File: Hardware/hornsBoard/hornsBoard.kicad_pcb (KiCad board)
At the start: 2 copper layers, 24 x 27 mm, 10 parts, among them J1 Conn_01x03, J2 Conn_01x02, J3 Conn_01x02, J4 Conn_01x02, Q2 IRF6785

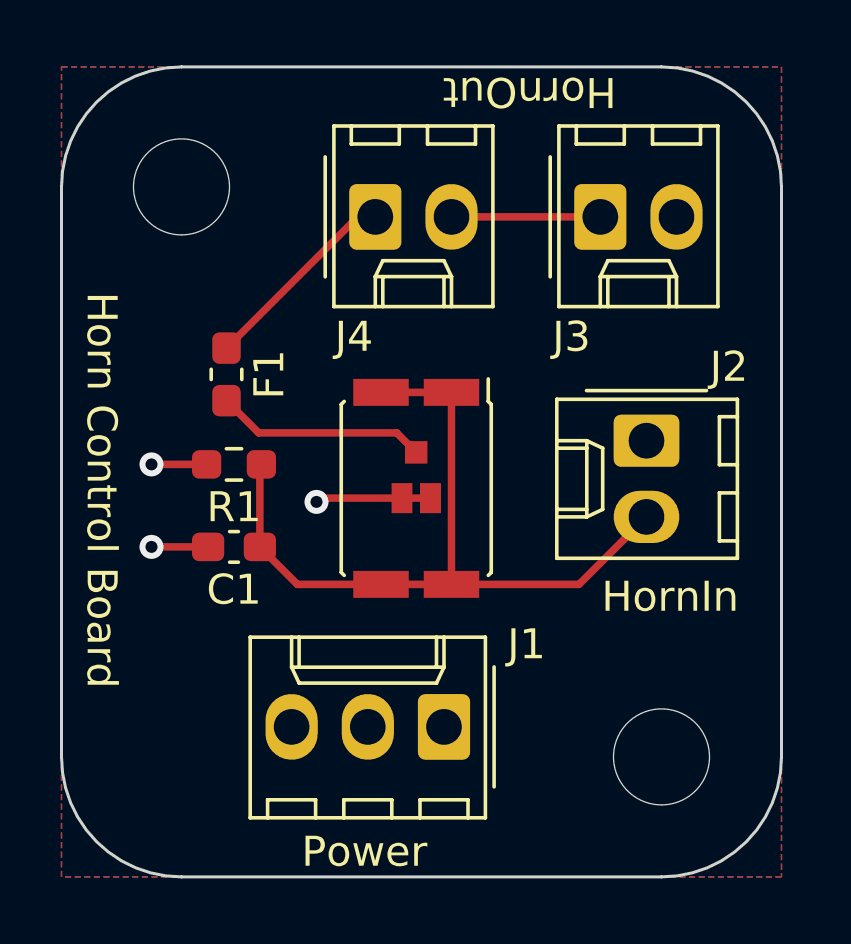
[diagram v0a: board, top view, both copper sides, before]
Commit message: reworked hornsBoard PCB
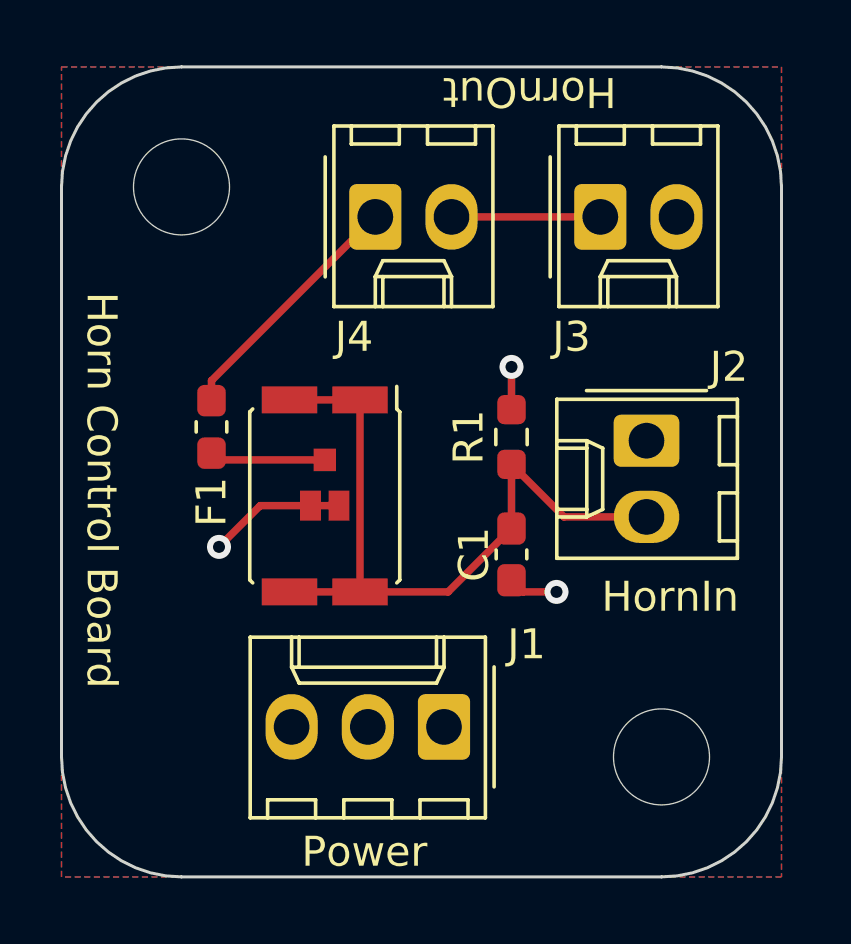
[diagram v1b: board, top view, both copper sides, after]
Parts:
- moved R1 9.29 mm to (153.0, 109.3), turned to 90 degrees
- moved C1 9.25 mm to (153.0, 113.2), turned to -90 degrees
- moved Q2 3.06 mm to (146.8, 111.3)
- moved F1 1.82 mm to (143.0, 109.0)
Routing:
- net Net-(Q2-G): track 7.04 -> 3.87 mm
- net Net-(J4-Pin_1): track 6.77 -> 8.97 mm
- net /Horn_Signal: track 25.9 -> 24.4 mm
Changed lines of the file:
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@@
   )
   (footprint "Resistor_SMD:R_0603_1608Metric_Pad0.98x0.95mm_HandSolder" (layer "F.Cu")
-    (at 143.75 110.25 180)
+    (at 153 109.3375 90)
     (descr "Resistor SMD 0603 (1608 Metric), square (rectangular) end terminal, IPC_7351 nominal with elongated pad for handsoldering. (Body size source: IPC-SM-782 page 72, https://www.pcb-3d.com/wordpress/wp-content/uploads/ipc-sm-782a_amendment_1_and_2.pdf), generated with kicad-footprint-generator")
     (tags "resistor handsolder")
@@
     (property "ki_keywords" "R res resistor")
     (attr smd)
-    (fp_text reference "R1" (at 0 -1.43) (layer "F.SilkS")
-        (effects (font (size 1 1) (thickness 0.15)))
-    )
-    (fp_text value "R_US" (at 0 1.43) (layer "F.Fab") hide
-        (effects (font (size 1 1) (thickness 0.15)))
-    )
-    (fp_text user "${REFERENCE}" (at 0 0) (layer "F.Fab")
+    (fp_text reference "R1" (at 0 -1.43 90) (layer "F.SilkS")
+        (effects (font (size 1 1) (thickness 0.15)))
+    )
+    (fp_text value "R_US" (at 0 1.43 90) (layer "F.Fab") hide
+        (effects (font (size 1 1) (thickness 0.15)))
+    )
+    (fp_text user "${REFERENCE}" (at 0 0 90) (layer "F.Fab")
         (effects (font (size 0.4 0.4) (thickness 0.06)))
     )
@@
     (fp_line (start 0.8 0.4125) (end -0.8 0.4125)
       (stroke (width 0.1) (type solid)) (layer "F.Fab"))
-    (pad "1" smd roundrect (at -0.9125 0 180) (size 0.975 0.95) (layers "F.Cu" "F.Paste" "F.Mask") (roundrect_rratio 0.25)
+    (pad "1" smd roundrect (at -0.9125 0 90) (size 0.975 0.95) (layers "F.Cu" "F.Paste" "F.Mask") (roundrect_rratio 0.25)
       (net 1 "/Horn_Signal") (pintype "passive"))
-    (pad "2" smd roundrect (at 0.9125 0 180) (size 0.975 0.95) (layers "F.Cu" "F.Paste" "F.Mask") (roundrect_rratio 0.25)
+    (pad "2" smd roundrect (at 0.9125 0 90) (size 0.975 0.95) (layers "F.Cu" "F.Paste" "F.Mask") (roundrect_rratio 0.25)
       (net 2 "GND") (pintype "passive"))
     (model "${KICAD6_3DMODEL_DIR}/Resistor_SMD.3dshapes/R_0603_1608Metric.wrl"
@@
   )
   (footprint "Capacitor_SMD:C_0603_1608Metric_Pad1.08x0.95mm_HandSolder" (layer "F.Cu")
-    (at 143.75 113 180)
+    (at 153 113.25 -90)
     (descr "Capacitor SMD 0603 (1608 Metric), square (rectangular) end terminal, IPC_7351 nominal with elongated pad for handsoldering. (Body size source: IPC-SM-782 page 76, https://www.pcb-3d.com/wordpress/wp-content/uploads/ipc-sm-782a_amendment_1_and_2.pdf), generated with kicad-footprint-generator")
     (tags "capacitor handsolder")
@@
     (property "ki_keywords" "cap capacitor")
     (attr smd)
-    (fp_text reference "C1" (at 0 -1.43) (layer "F.SilkS")
-        (effects (font (size 1 1) (thickness 0.15)))
-    )
-    (fp_text value "C" (at 0 1.43) (layer "F.Fab") hide
-        (effects (font (size 1 1) (thickness 0.15)))
-    )
-    (fp_text user "${REFERENCE}" (at 0 0) (layer "F.Fab")
+    (fp_text reference "C1" (at 0 1.25 -270) (layer "F.SilkS")
+        (effects (font (size 1 1) (thickness 0.15)))
+    )
+    (fp_text value "C" (at 0 1.43 -270) (layer "F.Fab") hide
+        (effects (font (size 1 1) (thickness 0.15)))
+    )
+    (fp_text user "${REFERENCE}" (at 0 0 -270) (layer "F.Fab")
         (effects (font (size 0.4 0.4) (thickness 0.06)))
     )
@@
     (fp_line (start 0.8 0.4) (end -0.8 0.4)
       (stroke (width 0.1) (type solid)) (layer "F.Fab"))
-    (pad "1" smd roundrect (at -0.8625 0 180) (size 1.075 0.95) (layers "F.Cu" "F.Paste" "F.Mask") (roundrect_rratio 0.25)
+    (pad "1" smd roundrect (at -0.8625 0 270) (size 1.075 0.95) (layers "F.Cu" "F.Paste" "F.Mask") (roundrect_rratio 0.25)
       (net 1 "/Horn_Signal") (pintype "passive"))
-    (pad "2" smd roundrect (at 0.8625 0 180) (size 1.075 0.95) (layers "F.Cu" "F.Paste" "F.Mask") (roundrect_rratio 0.25)
+    (pad "2" smd roundrect (at 0.8625 0 270) (size 1.075 0.95) (layers "F.Cu" "F.Paste" "F.Mask") (roundrect_rratio 0.25)
       (net 2 "GND") (pintype "passive"))
     (model "${KICAD6_3DMODEL_DIR}/Capacitor_SMD.3dshapes/C_0603_1608Metric.wrl"
@@
   )
   (footprint "Fuse:Fuse_0603_1608Metric_Pad1.05x0.95mm_HandSolder" (layer "F.Cu")
-    (at 143.5 107.25 -90)
+    (at 143 109 -90)
     (descr "Fuse SMD 0603 (1608 Metric), square (rectangular) end terminal, IPC_7351 nominal with elongated pad for handsoldering. (Body size source: http://www.tortai-tech.com/upload/download/2011102023233369053.pdf), generated with kicad-footprint-generator")
     (tags "fuse handsolder")
@@
     (property "ki_keywords" "fuse")
     (attr smd)
-    (fp_text reference "F1" (at 0 -1.43 90) (layer "F.SilkS")
+    (fp_text reference "F1" (at 2.5 0 90) (layer "F.SilkS")
         (effects (font (size 1 1) (thickness 0.15)))
     )
@@
   )
   (footprint "Package_DirectFET:DirectFET_MZ" (layer "F.Cu")
-    (at 149.825 111.05 -90)
+    (at 146.775 111.3 -90)
     (descr "DirectFET MZ https://www.infineon.com/dgdl/Infineon-AN-1035-ApplicationNotes-v29_01-EN.pdf?fileId=5546d462533600a40153559159020f76#page=31")
     (tags "DirectFET MZ MOSFET Infineon")
@@
     (effects (font (size 1 1) (thickness 0.15)) (justify left bottom))
   )
-  (segment (start 151 107.85) (end 148.65 107.85) (width 0.25) (layer "F.Cu") (net 1))
-  (segment (start 145.8625 114.25) (end 144.6125 113) (width 0.25) (layer "F.Cu") (net 1))
-  (segment (start 155.25 114.25) (end 157.5 112) (width 0.25) (layer "F.Cu") (net 1))
-  (segment (start 144.6125 113) (end 144.6125 110.3) (width 0.25) (layer "F.Cu") (net 1))
-  (segment (start 151 107.85) (end 151 114.25) (width 0.25) (layer "F.Cu") (net 1))
-  (segment (start 148.65 114.25) (end 145.8625 114.25) (width 0.25) (layer "F.Cu") (net 1))
-  (segment (start 148.65 114.25) (end 151 114.25) (width 0.25) (layer "F.Cu") (net 1))
-  (segment (start 144.6125 110.3) (end 144.6625 110.25) (width 0.25) (layer "F.Cu") (net 1))
-  (segment (start 151 114.25) (end 155.25 114.25) (width 0.25) (layer "F.Cu") (net 1))
-  (segment (start 146.625 111.375) (end 146.5 111.5) (width 0.25) (layer "F.Cu") (net 2))
-  (segment (start 142.8875 113) (end 141 113) (width 0.25) (layer "F.Cu") (net 2))
-  (segment (start 142.8375 110.25) (end 141 110.25) (width 0.25) (layer "F.Cu") (net 2))
-  (segment (start 149.35 111.375) (end 146.625 111.375) (width 0.25) (layer "F.Cu") (net 2))
-  (segment (start 150.3 111.375) (end 149.35 111.375) (width 0.25) (layer "F.Cu") (net 2))
-  (via (at 146.5 111.5) (size 0.8) (drill 0.4) (layers "F.Cu" "B.Cu") (free) (net 2))
-  (via (at 141 113) (size 0.8) (drill 0.4) (layers "F.Cu" "B.Cu") (free) (net 2))
-  (via (at 141 110.25) (size 0.8) (drill 0.4) (layers "F.Cu" "B.Cu") (free) (net 2))
+  (segment (start 150.8875 114.5) (end 147.95 114.5) (width 0.25) (layer "F.Cu") (net 1))
+  (segment (start 153 112.3875) (end 150.8875 114.5) (width 0.25) (layer "F.Cu") (net 1))
+  (segment (start 147.95 108.1) (end 147.95 114.5) (width 0.25) (layer "F.Cu") (net 1))
+  (segment (start 147.95 114.5) (end 145.6 114.5) (width 0.25) (layer "F.Cu") (net 1))
+  (segment (start 157.5 112) (end 154.75 112) (width 0.25) (layer "F.Cu") (net 1))
+  (segment (start 154.75 112) (end 153 110.25) (width 0.25) (layer "F.Cu") (net 1))
+  (segment (start 153 110.25) (end 153 112.3875) (width 0.25) (layer "F.Cu") (net 1))
+  (segment (start 145.6 108.1) (end 147.95 108.1) (width 0.25) (layer "F.Cu") (net 1))
+  (segment (start 153.3875 114.5) (end 153 114.1125) (width 0.25) (layer "F.Cu") (net 2))
+  (segment (start 146.3 111.625) (end 144.625 111.625) (width 0.25) (layer "F.Cu") (net 2))
+  (segment (start 153 108.425) (end 153 107) (width 0.25) (layer "F.Cu") (net 2))
+  (segment (start 154.5 114.5) (end 153.3875 114.5) (width 0.25) (layer "F.Cu") (net 2))
+  (segment (start 144.625 111.625) (end 143.25 113) (width 0.25) (layer "F.Cu") (net 2))
+  (segment (start 146.3 111.625) (end 147.25 111.625) (width 0.25) (layer "F.Cu") (net 2))
+  (via (at 143.25 113) (size 0.8) (drill 0.4) (layers "F.Cu" "B.Cu") (free) (net 2))
+  (via (at 154.5 114.5) (size 0.8) (drill 0.4) (layers "F.Cu" "B.Cu") (free) (net 2))
+  (via (at 153 107) (size 0.8) (drill 0.4) (layers "F.Cu" "B.Cu") (free) (net 2))
   (segment (start 147.875 102) (end 148.46 102) (width 0.25) (layer "F.Cu") (net 3))
-  (segment (start 143.5 106.375) (end 147.875 102) (width 0.25) (layer "F.Cu") (net 3))
-  (segment (start 149.825 109.85) (end 149.175 109.2) (width 0.25) (layer "F.Cu") (net 4))
-  (segment (start 144.575 109.2) (end 143.5 108.125) (width 0.25) (layer "F.Cu") (net 4))
-  (segment (start 149.175 109.2) (end 144.575 109.2) (width 0.25) (layer "F.Cu") (net 4))
+  (segment (start 143 108.125) (end 143 107.46) (width 0.25) (layer "F.Cu") (net 3))
+  (segment (start 143 107.46) (end 148.46 102) (width 0.25) (layer "F.Cu") (net 3))
+  (segment (start 143.225 110.1) (end 143 109.875) (width 0.25) (layer "F.Cu") (net 4))
+  (segment (start 146.775 110.1) (end 143.225 110.1) (width 0.25) (layer "F.Cu") (net 4))
   (segment (start 151 102) (end 155.96 102) (width 0.25) (layer "F.Cu") (net 6))
   (zone (net 5) (net_name "/24V") (layer "F.Cu") (hatch edge 0.5)
